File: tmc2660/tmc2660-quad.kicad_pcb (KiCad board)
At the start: 4 copper layers, 125 x 40 mm, 81 parts, among them J1 Power, J100 0R, J2 DataIn, J200 0R, J300 0R, J400 0R, M0 Mount, M1 Mount, M100 Mount, M101 Mount, M200 Mount, M201 Mount, M300 Mount, M301 Mount, M400 Mount, M401 Mount, P100 Motor, P200 Motor, P300 Motor, P400 Motor, U100 TMC2660, U200 TMC2660, U300 TMC2660, U400 TMC2660

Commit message: Fix some traces that unnecessarily have been pushed through copper fills.
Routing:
- net VCC: track 54.1 -> 57.0 mm
- net DIR4: track 110.4 -> 111.0 mm
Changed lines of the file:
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@@
     (thickness 1.6)
     (drawings 44)
-    (tracks 990)
+    (tracks 991)
     (zones 0)
     (modules 81)
@@
   )
   (setup
-    (last_trace_width 0.3)
+    (last_trace_width 1.2)
     (user_trace_width 0.2)
     (user_trace_width 0.3)
@@
   (via (at 177.867 79.351) (size 0.9) (drill 0.5) (layers F.Cu B.Cu) (net 2))
   (via (at 180.407 78.081) (size 0.9) (drill 0.5) (layers F.Cu B.Cu) (net 2))
-  (segment (start 69.3915 61.718686) (end 69.3915 71.165462) (width 1.2) (layer In2.Cu) (net 3))
-  (segment (start 69.3915 71.165462) (end 75.442038 77.216) (width 1.2) (layer In2.Cu) (net 3))
-  (segment (start 66.3385 59.887) (end 67.559814 59.887) (width 1.2) (layer In2.Cu) (net 3))
-  (segment (start 67.559814 59.887) (end 69.3915 61.718686) (width 1.2) (layer In2.Cu) (net 3))
-  (segment (start 75.442038 77.216) (end 83.82 77.216) (width 1.2) (layer In2.Cu) (net 3))
+  (segment (start 70.6395 77.216) (end 69.3915 75.968) (width 1.2) (layer In2.Cu) (net 3))
+  (segment (start 83.82 77.216) (end 70.6395 77.216) (width 1.1) (layer In2.Cu) (net 3))
+  (segment (start 69.3915 75.968) (end 69.3915 61.718686) (width 1.2) (layer In2.Cu) (net 3))
+  (segment (start 69.3915 61.718686) (end 67.559814 59.887) (width 1.2) (layer In2.Cu) (net 3))
+  (segment (start 67.559814 59.887) (end 66.3385 59.887) (width 1.2) (layer In2.Cu) (net 3))
   (segment (start 80.5565 71.636) (end 80.5565 73.3515) (width 0.4) (layer F.Cu) (net 13))
   (segment (start 80.5565 73.3515) (end 79.994 73.914) (width 0.4) (layer F.Cu) (net 13))
@@
   (segment (start 155.5565 71.636) (end 155.5565 73.3515) (width 0.4) (layer F.Cu) (net 61))
   (segment (start 155.5565 73.3515) (end 154.994 73.914) (width 0.4) (layer F.Cu) (net 61))
-  (segment (start 87.1715 75.057) (end 90.4735 75.057) (width 0.25) (layer In1.Cu) (net 63))
-  (segment (start 101.5225 74.041) (end 115.3655 74.041) (width 0.25) (layer In1.Cu) (net 63))
-  (segment (start 163.778608 71.75302) (end 164.344293 71.75302) (width 0.25) (layer In1.Cu) (net 63))
-  (segment (start 86.2825 74.168) (end 87.1715 75.057) (width 0.25) (layer In1.Cu) (net 63))
-  (segment (start 135.9395 73.152) (end 140.1305 73.152) (width 0.25) (layer In1.Cu) (net 63))
-  (segment (start 74.8525 74.168) (end 86.2825 74.168) (width 0.25) (layer In1.Cu) (net 63))
-  (segment (start 99.1095 71.628) (end 101.5225 74.041) (width 0.25) (layer In1.Cu) (net 63))
-  (segment (start 117.3975 72.009) (end 134.7965 72.009) (width 0.25) (layer In1.Cu) (net 63))
-  (segment (start 93.9025 71.628) (end 99.1095 71.628) (width 0.25) (layer In1.Cu) (net 63))
-  (segment (start 71.3535 77.667) (end 74.8525 74.168) (width 0.25) (layer In1.Cu) (net 63))
+  (segment (start 74.8525 74.1265) (end 74.235 73.509) (width 0.25) (layer In1.Cu) (net 63))
+  (segment (start 135.9395 73.152) (end 134.7965 72.009) (width 0.25) (layer In1.Cu) (net 63))
+  (segment (start 87.1715 75.057) (end 86.2825 74.168) (width 0.25) (layer In1.Cu) (net 63))
+  (segment (start 74.8525 74.168) (end 74.8525 74.1265) (width 0.25) (layer In1.Cu) (net 63))
+  (segment (start 140.1305 73.152) (end 135.9395 73.152) (width 0.25) (layer In1.Cu) (net 63))
+  (segment (start 90.4735 75.057) (end 87.1715 75.057) (width 0.25) (layer In1.Cu) (net 63))
+  (segment (start 93.9025 71.628) (end 90.4735 75.057) (width 0.25) (layer In1.Cu) (net 63))
+  (segment (start 99.1095 71.628) (end 93.9025 71.628) (width 0.25) (layer In1.Cu) (net 63))
+  (segment (start 74.235 73.509) (end 70.4965 73.509) (width 0.25) (layer In1.Cu) (net 63))
+  (segment (start 134.7965 72.009) (end 117.3975 72.009) (width 0.25) (layer In1.Cu) (net 63))
+  (segment (start 86.2825 74.168) (end 74.8525 74.168) (width 0.25) (layer In1.Cu) (net 63))
+  (segment (start 101.5225 74.041) (end 99.1095 71.628) (width 0.25) (layer In1.Cu) (net 63))
+  (segment (start 115.3655 74.041) (end 101.5225 74.041) (width 0.25) (layer In1.Cu) (net 63))
+  (segment (start 141.52948 71.75302) (end 140.1305 73.152) (width 0.25) (layer In1.Cu) (net 63))
+  (segment (start 164.344293 71.75302) (end 141.52948 71.75302) (width 0.25) (layer In1.Cu) (net 63))
+  (segment (start 117.3975 72.009) (end 115.3655 74.041) (width 0.25) (layer In1.Cu) (net 63))
+  (segment (start 70.4965 73.509) (end 66.3385 77.667) (width 0.25) (layer In1.Cu) (net 63))
   (segment (start 164.344293 72.401045) (end 164.344293 72.318705) (width 0.3) (layer F.Cu) (net 63))
   (segment (start 160.86651 73.24601) (end 163.499328 73.24601) (width 0.3) (layer F.Cu) (net 63))
@@
   (segment (start 164.344293 72.318705) (end 164.344293 71.75302) (width 0.3) (layer F.Cu) (net 63))
   (segment (start 160.3565 72.736) (end 160.86651 73.24601) (width 0.3) (layer F.Cu) (net 63))
-  (segment (start 90.4735 75.057) (end 93.9025 71.628) (width 0.25) (layer In1.Cu) (net 63))
-  (segment (start 66.3385 77.667) (end 71.3535 77.667) (width 0.25) (layer In1.Cu) (net 63))
   (via (at 164.344293 71.75302) (size 0.8) (drill 0.4) (layers F.Cu B.Cu) (net 63))
-  (segment (start 134.7965 72.009) (end 135.9395 73.152) (width 0.25) (layer In1.Cu) (net 63))
-  (segment (start 115.3655 74.041) (end 117.3975 72.009) (width 0.25) (layer In1.Cu) (net 63))
-  (segment (start 140.1305 73.152) (end 141.52948 71.75302) (width 0.25) (layer In1.Cu) (net 63))
-  (segment (start 141.52948 71.75302) (end 163.778608 71.75302) (width 0.25) (layer In1.Cu) (net 63))
   (segment (start 163.499328 73.24601) (end 164.344293 72.401045) (width 0.3) (layer F.Cu) (net 63))
   (segment (start 163.747304 70.866) (end 163.894458 70.718846) (width 0.25) (layer In1.Cu) (net 64))
@@
     (polygon
       (pts
-        (xy 159.833 77.446) (xy 75.1065 77.597) (xy 75.1065 76.581) (xy 159.833 76.43)
+        (xy 159.833 77.446) (xy 70.8695 77.6365) (xy 70.8695 76.6205) (xy 159.833 76.43)
       )
     )

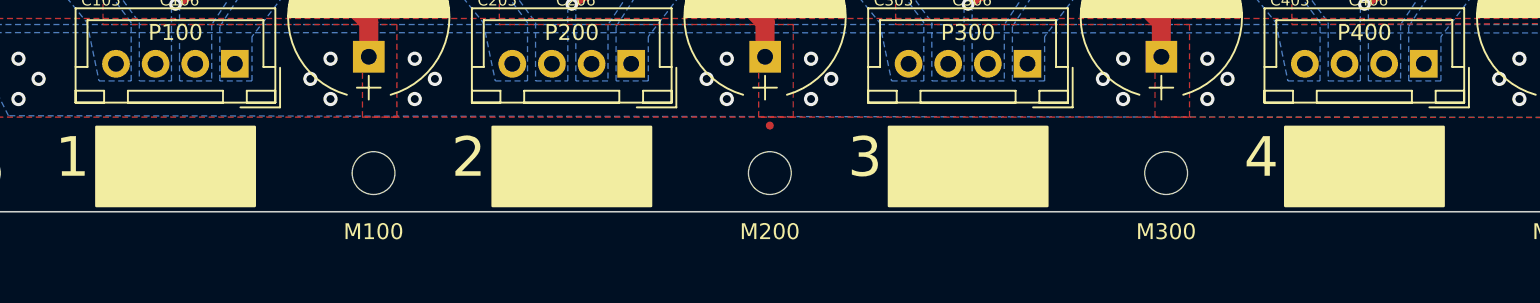
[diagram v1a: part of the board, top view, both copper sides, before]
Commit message: Replace polygons with zones that are less broken objects.
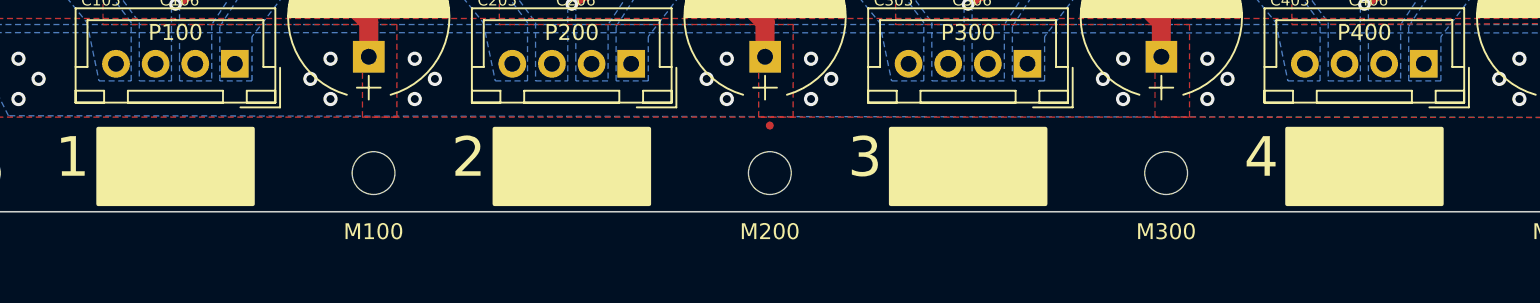
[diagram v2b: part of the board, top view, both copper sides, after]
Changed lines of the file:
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@@
-(kicad_pcb (version 20170922) (host pcbnew "(2017-11-18 revision ff5ee05de)-master")
+(kicad_pcb (version 20170922) (host pcbnew "(2017-11-20 revision 422b7dd55)-master")
   (general
     (thickness 1.6)
-    (drawings 44)
+    (drawings 40)
     (tracks 991)
     (zones 0)
@@
   )
   (setup
-    (last_trace_width 1.2)
+    (last_trace_width 0.25)
     (user_trace_width 0.2)
     (user_trace_width 0.3)
@@
     (effects (font (size 1.5 1.5) (thickness 0.3)) (justify mirror))
   )
-  (gr_poly (pts (xy 78.8235 83.1605) (xy 88.8235 83.1605) (xy 88.8235 88.1605) (xy 78.8235 88.1605)) (layer F.SilkS) (width 0.15))
-  (gr_poly (pts (xy 153.8235 83.1605) (xy 163.8235 83.1605) (xy 163.8235 88.1605) (xy 153.8235 88.1605)) (layer F.SilkS) (width 0.15))
-  (gr_poly (pts (xy 128.8235 83.1605) (xy 138.8235 83.1605) (xy 138.8235 88.1605) (xy 128.8235 88.1605)) (layer F.SilkS) (width 0.15))
-  (gr_poly (pts (xy 103.8235 83.1605) (xy 113.8235 83.1605) (xy 113.8235 88.1605) (xy 103.8235 88.1605)) (layer F.SilkS) (width 0.15))
   (gr_line (start 170.882 61.571) (end 184.217 61.571) (layer F.SilkS) (width 1))
   (gr_text GND (at 171.517 57.634 90) (layer F.SilkS)
@@
       )
     )
+  )
+  (zone (net 0) (net_name "") (layer F.SilkS) (hatch edge 0.508)
+    (connect_pads (clearance 0.254))
+    (min_thickness 0.254)
+    (fill yes (arc_segments 16) (thermal_gap 0.508) (thermal_bridge_width 0.508))
+    (polygon
+      (pts
+        (xy 78.8235 83.1605) (xy 88.8235 83.1605) (xy 88.8235 88.1605) (xy 78.8235 88.1605)
+      )
+    )
+  )
+  (zone (net 0) (net_name "") (layer F.SilkS) (hatch edge 0.508)
+    (connect_pads (clearance 0.254))
+    (min_thickness 0.254)
+    (fill yes (arc_segments 16) (thermal_gap 0.508) (thermal_bridge_width 0.508))
+    (polygon
+      (pts
+        (xy 103.8235 83.1605) (xy 113.8235 83.1605) (xy 113.8235 88.1605) (xy 103.8235 88.1605)
+      )
+    )
+  )
+  (zone (net 0) (net_name "") (layer F.SilkS) (hatch edge 0.508)
+    (connect_pads (clearance 0.254))
+    (min_thickness 0.254)
+    (fill yes (arc_segments 16) (thermal_gap 0.508) (thermal_bridge_width 0.508))
+    (polygon
+      (pts
+        (xy 128.8235 83.1605) (xy 138.8235 83.1605) (xy 138.8235 88.1605) (xy 128.8235 88.1605)
+      )
+    )
+  )
+  (zone (net 0) (net_name "") (layer F.SilkS) (hatch edge 0.508)
+    (connect_pads (clearance 0.254))
+    (min_thickness 0.254)
+    (fill yes (arc_segments 16) (thermal_gap 0.508) (thermal_bridge_width 0.508))
+    (polygon
+      (pts
+        (xy 153.8235 83.1605) (xy 163.8235 83.1605) (xy 163.8235 88.1605) (xy 153.8235 88.1605)
+      )
+    )

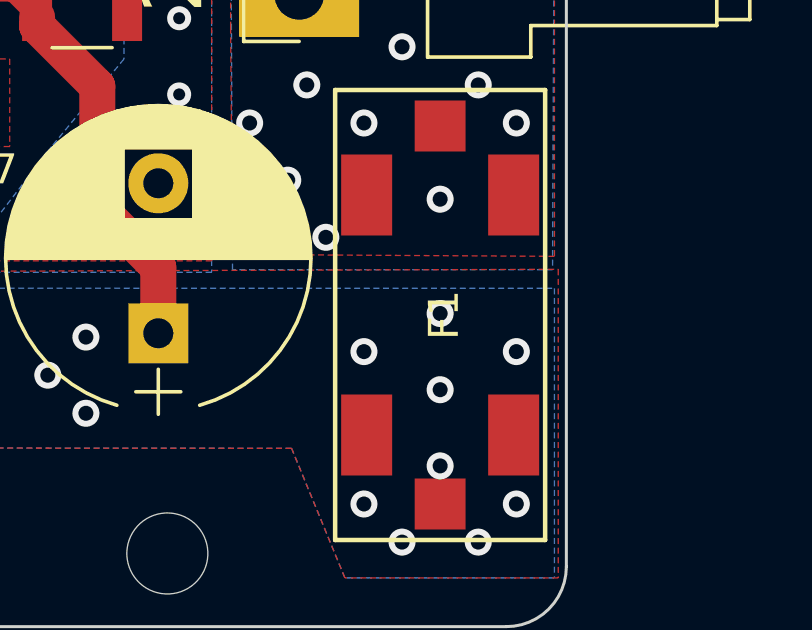
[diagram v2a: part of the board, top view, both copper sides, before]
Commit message: Rename local *.pretty to project name.
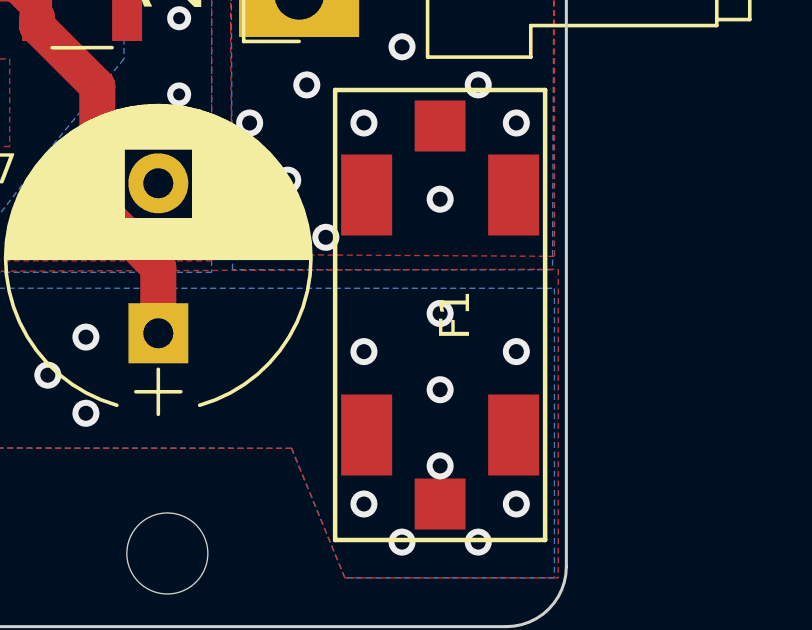
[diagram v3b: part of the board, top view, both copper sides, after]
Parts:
- F1: footprint Fuses:BladeFuse-Mini_Keystone-3586 -> Quadrigotion:BladeFuse-Mini_Keystone-3586
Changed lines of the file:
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@@
     (add_net VMot)
+  )
+  (module Quadrigotion:BladeFuse-Mini_Keystone-3586 (layer F.Cu)
+    (at 180.407 78.131 90)
+    (fp_text reference F1 (at 0 0.5 90) (layer F.SilkS)
+      (effects (font (size 1 1) (thickness 0.15)))
+    )
+    (fp_text value Fuse (at 0 -0.5 90) (layer F.Fab)
+      (effects (font (size 1 1) (thickness 0.15)))
+    )
+    (fp_line (start -7.5 -3.5) (end 7.5 -3.5) (layer F.SilkS) (width 0.15))
+    (fp_line (start 7.5 -3.5) (end 7.5 3.5) (layer F.SilkS) (width 0.15))
+    (fp_line (start 7.5 3.5) (end -7.5 3.5) (layer F.SilkS) (width 0.15))
+    (fp_line (start -7.5 3.5) (end -7.5 -3.5) (layer F.SilkS) (width 0.15))
+    (pad 1 smd rect (at -6.3 0 90) (size 1.7 1.7) (layers F.Cu F.Paste F.Mask)
+      (net 2 VMot))
+    (pad 2 smd rect (at 6.3 0 90) (size 1.7 1.7) (layers F.Cu F.Paste F.Mask)
+      (net 69 /PowerIn))
+    (pad 2 smd rect (at 4 2.45 90) (size 2.7 1.7) (layers F.Cu F.Paste F.Mask)
+      (net 69 /PowerIn))
+    (pad 2 smd rect (at 4 -2.45 90) (size 2.7 1.7) (layers F.Cu F.Paste F.Mask)
+      (net 69 /PowerIn))
+    (pad 1 smd rect (at -4 -2.45 90) (size 2.7 1.7) (layers F.Cu F.Paste F.Mask)
+      (net 2 VMot))
+    (pad 1 smd rect (at -4 2.45 90) (size 2.7 1.7) (layers F.Cu F.Paste F.Mask)
+      (net 2 VMot))
   )
   (module Fiducials:Fiducial_0.5mm_Dia_1mm_Outer locked (layer F.Cu)
@@
       (xy 0.555814 -2.531069)) (layer F.SilkS) (width 0.01))
   )
-  (module Fuses:BladeFuse-Mini_Keystone-3586 (layer F.Cu)
-    (at 180.407 78.131 90)
-    (fp_text reference F1 (at 0 0.127 90) (layer F.SilkS)
-      (effects (font (size 1 1) (thickness 0.15)))
-    )
-    (fp_text value Fuse (at -5.588 -4.445 90) (layer F.Fab)
-      (effects (font (size 1 1) (thickness 0.15)))
-    )
-    (fp_line (start -7.5 -3.5) (end 7.5 -3.5) (layer F.SilkS) (width 0.15))
-    (fp_line (start 7.5 -3.5) (end 7.5 3.5) (layer F.SilkS) (width 0.15))
-    (fp_line (start 7.5 3.5) (end -7.5 3.5) (layer F.SilkS) (width 0.15))
-    (fp_line (start -7.5 3.5) (end -7.5 -3.5) (layer F.SilkS) (width 0.15))
-    (pad 1 smd rect (at -6.3 0 90) (size 1.7 1.7) (layers F.Cu F.Paste F.Mask)
-      (net 2 VMot))
-    (pad 2 smd rect (at 6.3 0 90) (size 1.7 1.7) (layers F.Cu F.Paste F.Mask)
-      (net 69 /PowerIn))
-    (pad 2 smd rect (at 4 2.45 90) (size 2.7 1.7) (layers F.Cu F.Paste F.Mask)
-      (net 69 /PowerIn))
-    (pad 2 smd rect (at 4 -2.45 90) (size 2.7 1.7) (layers F.Cu F.Paste F.Mask)
-      (net 69 /PowerIn))
-    (pad 1 smd rect (at -4 -2.45 90) (size 2.7 1.7) (layers F.Cu F.Paste F.Mask)
-      (net 2 VMot))
-    (pad 1 smd rect (at -4 2.45 90) (size 2.7 1.7) (layers F.Cu F.Paste F.Mask)
-      (net 2 VMot))
-  )
   (module Mounting_Holes:MountingHole_2.7mm_M2.5 (layer F.Cu)
